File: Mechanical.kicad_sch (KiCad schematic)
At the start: 3 parts, among them J3 Screw_Terminal_01x02, J5 Screw_Terminal_01x02, U5 L293D

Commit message: Started to layout PCB
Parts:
- removed J3, J5: Screw_Terminal_01x02, TerminalBlock:TerminalBlock_Altech_AK300-2_P5.00mm, symbol Connector:Screw_Terminal_01x02
- removed U5: L293D, Package_DIP:DIP-16_W7.62mm, symbol Driver_Motor:L293D
- added H1, H2, H3, H5: MountingHole, MountingHole:MountingHole_2.2mm_M2, symbol Mechanical:MountingHole
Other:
- title: Motor -> Mechanical

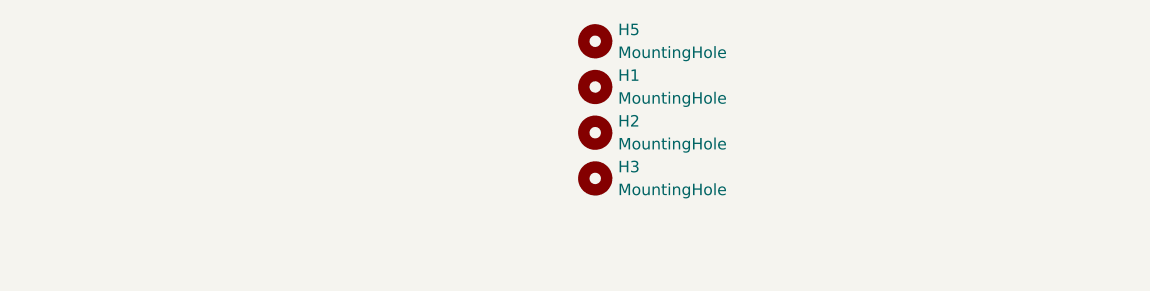
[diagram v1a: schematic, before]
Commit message: Placed all components on PCB
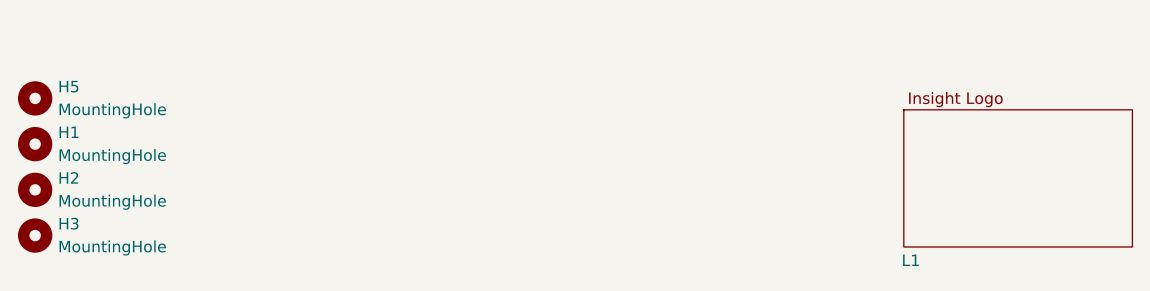
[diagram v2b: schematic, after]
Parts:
- added L1: ~, Insight Logo:Insight_Logo, symbol Insight Logo:Insight_Logo
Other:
- moved on the sheet: H1, H2, H3, H5
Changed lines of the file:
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@@
 	(symbol
 		(lib_id "Mechanical:MountingHole")
-		(at 130.81 97.79 0)
+		(at 68.58 104.14 0)
 		(unit 1)
 		(exclude_from_sim yes)
@@
 		(fields_autoplaced yes)
 		(property "Reference" "H2"
-			(at 133.35 96.5199 0)
+			(at 71.12 102.8699 0)
 			(effects
 				(font
@@
 		)
 		(property "Value" "MountingHole"
-			(at 133.35 99.0599 0)
+			(at 71.12 105.4099 0)
 			(effects
 				(font
@@
 		)
 		(property "Footprint" "MountingHole:MountingHole_2.2mm_M2"
-			(at 130.81 97.79 0)
+			(at 68.58 104.14 0)
 			(effects
 				(font
@@
 		)
 		(property "Datasheet" "~"
-			(at 130.81 97.79 0)
+			(at 68.58 104.14 0)
 			(effects
 				(font
@@
 		)
 		(property "Description" "Mounting Hole without connection"
-			(at 130.81 97.79 0)
+			(at 68.58 104.14 0)
 			(effects
 				(font
@@
 	(symbol
 		(lib_id "Mechanical:MountingHole")
-		(at 130.81 87.63 0)
+		(at 68.58 93.98 0)
 		(unit 1)
 		(exclude_from_sim yes)
@@
 		(fields_autoplaced yes)
 		(property "Reference" "H5"
-			(at 133.35 86.3599 0)
+			(at 71.12 92.7099 0)
 			(effects
 				(font
@@
 		)
 		(property "Value" "MountingHole"
-			(at 133.35 88.8999 0)
+			(at 71.12 95.2499 0)
 			(effects
 				(font
@@
 		)
 		(property "Footprint" "MountingHole:MountingHole_2.2mm_M2"
-			(at 130.81 87.63 0)
+			(at 68.58 93.98 0)
 			(effects
 				(font
@@
 		)
 		(property "Datasheet" "~"
-			(at 130.81 87.63 0)
+			(at 68.58 93.98 0)
 			(effects
 				(font
@@
 		)
 		(property "Description" "Mounting Hole without connection"
-			(at 130.81 87.63 0)
+			(at 68.58 93.98 0)
 			(effects
 				(font
@@
 	)
 	(symbol
+		(lib_id "Insight Logo:Insight_Logo")
+		(at 176.53 102.87 0)
+		(unit 1)
+		(exclude_from_sim no)
+		(in_bom yes)
+		(on_board yes)
+		(dnp no)
+		(property "Reference" "L1"
+			(at 164.846 112.014 0)
+			(effects
+				(font
+					(size 1.27 1.27)
+				)
+				(justify left)
+			)
+		)
+		(property "Value" "~"
+			(at 183.134 91.1437 0)
+			(effects
+				(font
+					(size 1.27 1.27)
+				)
+				(hide yes)
+			)
+		)
+		(property "Footprint" "Insight Logo:Insight_Logo"
+			(at 177.8 108.966 0)
+			(do_not_autoplace yes)
+			(effects
+				(font
+					(size 1.27 1.27)
+				)
+				(hide yes)
+			)
+		)
+		(property "Datasheet" ""
+			(at 170.688 93.98 0)
+			(effects
+				(font
+					(size 1.27 1.27)
+				)
+				(hide yes)
+			)
+		)
+		(property "Description" ""
+			(at 170.688 93.98 0)
+			(effects
+				(font
+					(size 1.27 1.27)
+				)
+				(hide yes)
+			)
+		)
+		(instances
+			(project ""
+				(path "/32966cbd-337b-4fa7-b66f-bfe62b1c18c3/bcb33c5c-ad1b-4b20-95a2-055bafcbbda2"
+					(reference "L1")
+					(unit 1)
+				)
+			)
+		)
+	)
+	(symbol
 		(lib_id "Mechanical:MountingHole")
-		(at 130.81 102.87 0)
+		(at 68.58 109.22 0)
 		(unit 1)
 		(exclude_from_sim yes)
@@
 		(fields_autoplaced yes)
 		(property "Reference" "H3"
-			(at 133.35 101.5999 0)
+			(at 71.12 107.9499 0)
 			(effects
 				(font
@@
 		)
 		(property "Value" "MountingHole"
-			(at 133.35 104.1399 0)
+			(at 71.12 110.4899 0)
 			(effects
 				(font
@@
 		)
 		(property "Footprint" "MountingHole:MountingHole_2.2mm_M2"
-			(at 130.81 102.87 0)
+			(at 68.58 109.22 0)
 			(effects
 				(font
@@
 		)
 		(property "Datasheet" "~"
-			(at 130.81 102.87 0)
+			(at 68.58 109.22 0)
 			(effects
 				(font
@@
 		)
 		(property "Description" "Mounting Hole without connection"
-			(at 130.81 102.87 0)
+			(at 68.58 109.22 0)
 			(effects
 				(font
@@
 	(symbol
 		(lib_id "Mechanical:MountingHole")
-		(at 130.81 92.71 0)
+		(at 68.58 99.06 0)
 		(unit 1)
 		(exclude_from_sim yes)
@@
 		(fields_autoplaced yes)
 		(property "Reference" "H1"
-			(at 133.35 91.4399 0)
+			(at 71.12 97.7899 0)
 			(effects
 				(font
@@
 		)
 		(property "Value" "MountingHole"
-			(at 133.35 93.9799 0)
+			(at 71.12 100.3299 0)
 			(effects
 				(font
@@
 		)
 		(property "Footprint" "MountingHole:MountingHole_2.2mm_M2"
-			(at 130.81 92.71 0)
+			(at 68.58 99.06 0)
 			(effects
 				(font
@@
 		)
 		(property "Datasheet" "~"
-			(at 130.81 92.71 0)
+			(at 68.58 99.06 0)
 			(effects
 				(font
@@
 		)
 		(property "Description" "Mounting Hole without connection"
-			(at 130.81 92.71 0)
-			(effects
-				(font
+			(at 68.58 99.06 0)
+			(effects
+				(font

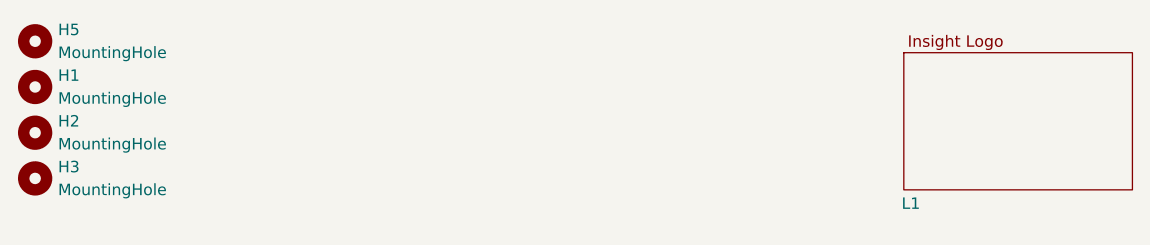
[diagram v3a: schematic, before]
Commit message: Updated PCB to be smaller and support stepper
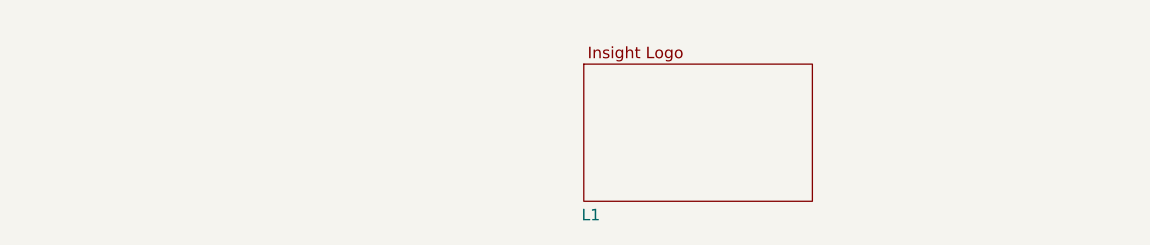
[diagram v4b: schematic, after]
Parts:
- removed H1, H2, H3, H5: MountingHole, MountingHole:MountingHole_2.2mm_M2, symbol Mechanical:MountingHole
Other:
- moved on the sheet: L1

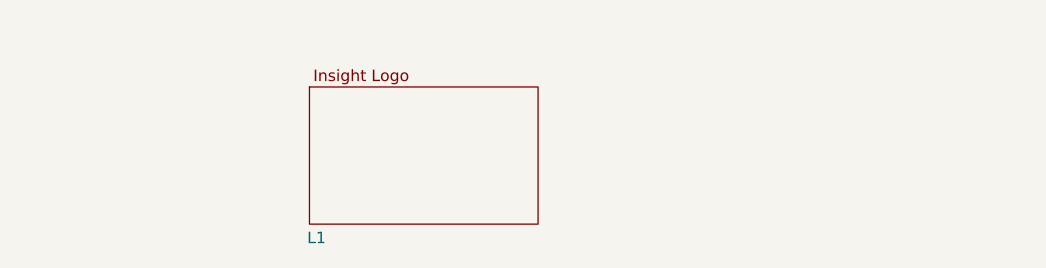
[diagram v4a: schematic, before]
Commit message: Updated to use boost converters
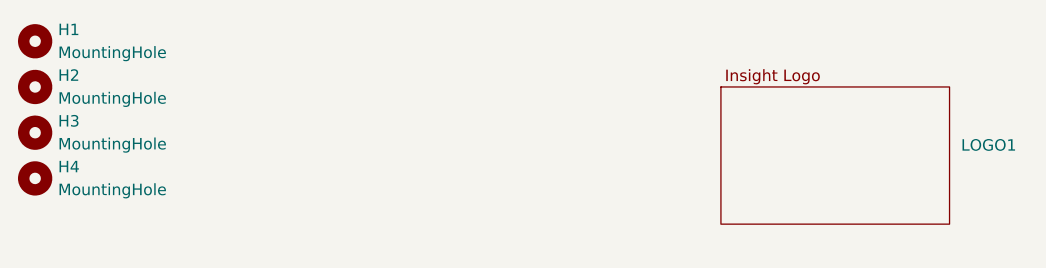
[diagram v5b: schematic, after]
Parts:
- removed L1: ~, Insight Logo:Insight_Logo, symbol Insight Logo:Insight_Logo
- added H1, H2, H3, H4: MountingHole, MountingHole:MountingHole_2.2mm_M2, symbol Mechanical:MountingHole
- added LOGO1: ~, Insight:Insight_Logo, symbol Insight:Insight_Logo
